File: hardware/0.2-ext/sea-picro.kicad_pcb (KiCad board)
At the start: 4 copper layers, 17.8 x 33 mm, 54 parts, among them J1 USB_C_Receptacle_USB2.0, J2 0.1" x 12, J3 0.1" x 12, J4 D+, J5 D-, J6 0.1" x 5, Q1 2N7002VC-7, Q2 2N7002VC-7, U1 ME6211C33M5G-N, U2 GD25Q64CWIGR, U3 RP2040, Y1 12MHz

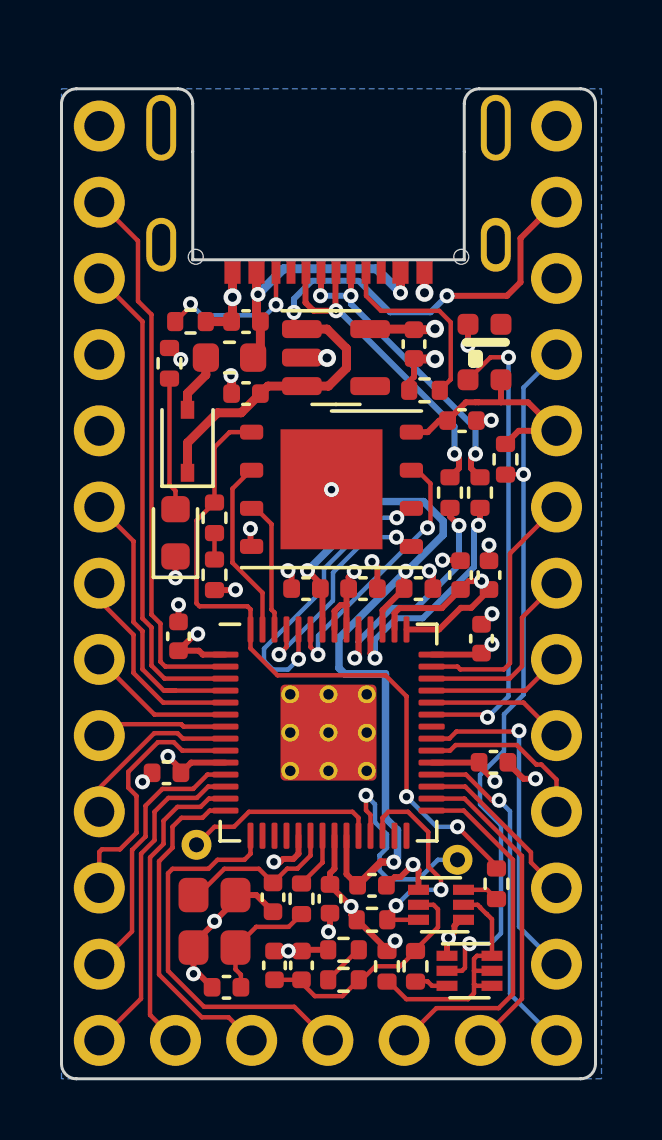
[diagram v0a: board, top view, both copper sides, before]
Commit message: add usb vbus detect
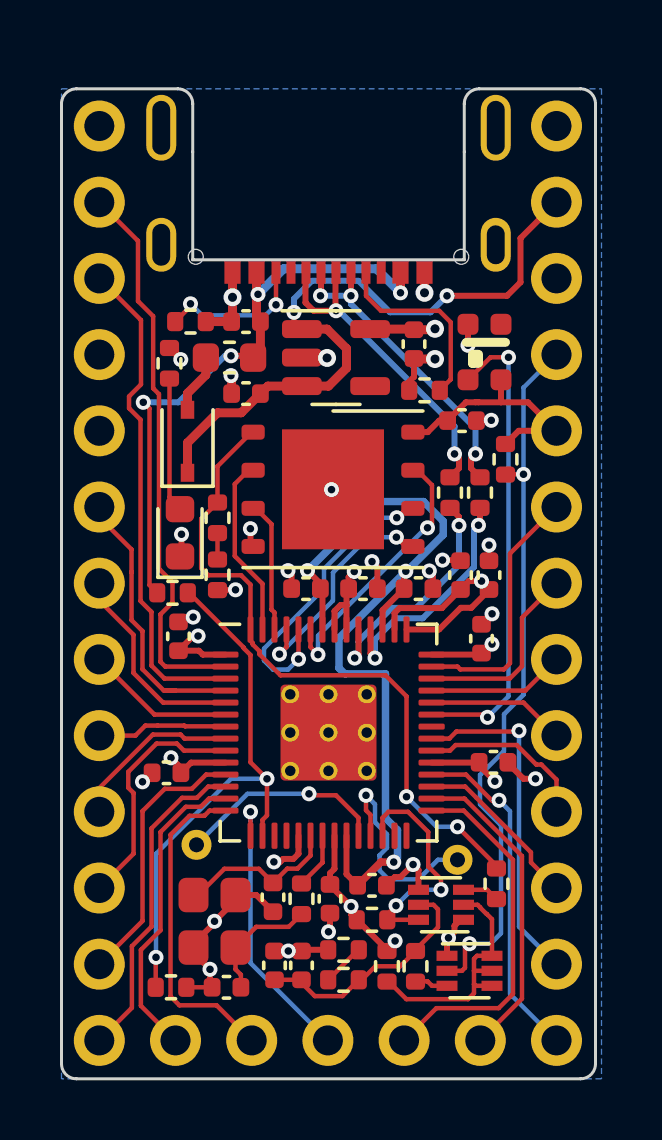
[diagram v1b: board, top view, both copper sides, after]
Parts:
- added R16: 2K2, Resistor_SMD:R_0402_1005Metric, F.Cu at (121.0, 91.6)
- added R17: 5K1, Resistor_SMD:R_0402_1005Metric, F.Cu at (121.0, 104.8)
- R3: value 1K -> 2K2
- moved D2 0.15 mm to (121.2, 89.6)
- moved R10 0.10 mm to (122.5, 89.1)
- moved R6 0.10 mm to (122.5, 91.0)
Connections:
- U3 pad 16: unconnected-(U3-Pad16) -> /VBUS_DETECT
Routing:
- net /VBUS_DETECT: track 0.00 -> 18.5 mm, vias 0 -> 2
- net VBUS: track 9.15 -> 20.0 mm, vias 2 -> 4
- net /15: track 13.2 -> 9.49 mm, vias 0 -> 1
- net /FLASH_nCS: track 23.3 -> 22.4 mm
- net GND: track 28.1 -> 28.8 mm
- net /SWDCLK: track 6.54 -> 7.03 mm, vias 0 -> 1

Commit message: add LED driver and more test points
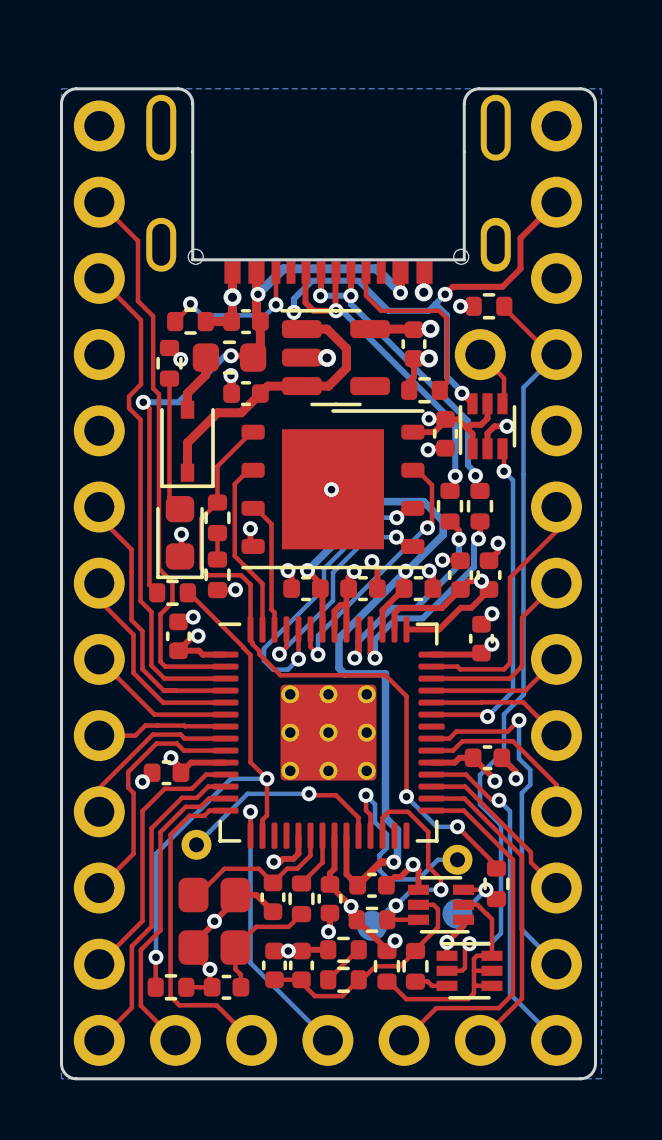
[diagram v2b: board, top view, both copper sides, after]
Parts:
- removed D3: WS2812C-2020, josh-led:WS2812C-2020
- added J7: 2.54, josh-connectors:PinHeader_1x01_P2.54mm_Circle, F.Cu at (131.3, 83.7)
- added TP3: nRST, josh-test-point:TestPoint_SMDPad_D1.0mm_NO_SILK, B.Cu at (127.7, 102.7)
- added TP4: BOOT, josh-test-point:TestPoint_SMDPad_D1.0mm_NO_SILK, B.Cu at (130.5, 102.3)
- added U4: 74LVC1T45Z6-7, Package_TO_SOT_SMD:SOT-563, F.Cu at (131.5, 86.0)
- moved R4 5.13 mm to (131.6, 82.0), turned to 0 degrees
- moved C4 0.70 mm to (130.1, 86.3), turned to -90 degrees
- moved R7 0.45 mm to (130.2, 88.7)
- moved R8 0.45 mm to (131.2, 88.7)
- moved C14 0.25 mm to (131.5, 97.1)
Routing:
- net /LED_DO: track 15.9 -> 11.3 mm
- net +5V: track 22.7 -> 26.2 mm, vias 2 -> 3
- net +3V3: track 36.9 -> 33.8 mm, vias 11 -> 13
- net Net-(J7-Pad1): track 0.00 -> 1.97 mm
- net /SWITCH: track 23.9 -> 25.8 mm, vias 2 -> 1
- net /BOOT: track 1.23 -> 2.51 mm, vias 0 -> 1
- net /nRST: track 7.94 -> 9.02 mm
- net /23_MOSI: track 11.3 -> 12.0 mm
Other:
- board text added: "25"
- board text added: "B"
- board text added: "R"

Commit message: update vscore markings
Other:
- board text added: "<- V score along these lines -> note USB connector sticks out 2mm"
- board text removed: "<- Vscore along -> these edges if panelising"
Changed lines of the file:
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@@
   (gr_line (start 119.75 77.25) (end 119.25 76.75) (layer "B.SilkS") (width 0.15))
   (gr_line (start 133.15 76.7) (end 132.95 76.9) (layer "B.SilkS") (width 0.15))
-  (gr_line (start 135.1 68.5) (end 135.1 114) (layer "Dwgs.User") (width 0.1))
-  (gr_line (start 117.3 68.5) (end 117.3 114) (layer "Dwgs.User") (width 0.1))
+  (gr_line (start 112 107.8) (end 136 107.8) (layer "Dwgs.User") (width 0.1))
+  (gr_line (start 112 74.8) (end 136 74.8) (layer "Dwgs.User") (width 0.1))
   (gr_line (start 117.3 75.3) (end 117.3 107.3) (layer "Edge.Cuts") (width 0.1))
   (gr_line (start 117.8 107.8) (end 134.6 107.8) (layer "Edge.Cuts") (width 0.1))
@@
     (effects (font (size 1 1) (thickness 0.15)) (justify mirror))
   )
-  (gr_text "<- Vscore along ->\nthese edges if\npanelising" (at 126.1 70.7) (layer "Dwgs.User")
+  (gr_text "<- V score along these lines ->\nnote USB connector sticks out 2mm" (at 114.2 91 90) (layer "Dwgs.User")
     (effects (font (size 1 1) (thickness 0.15)))
   )

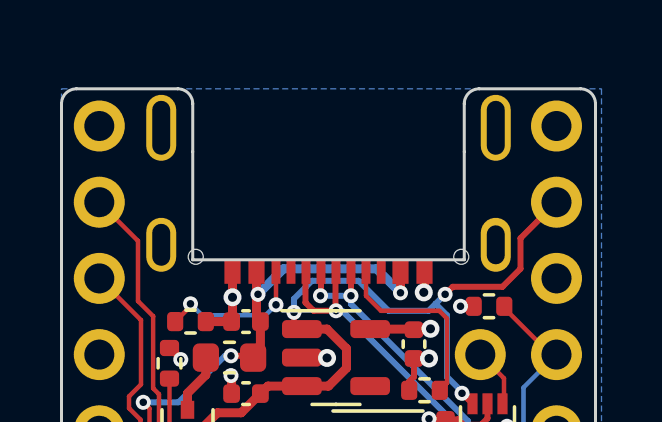
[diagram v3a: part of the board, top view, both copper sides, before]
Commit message: update ldo caps to 1u
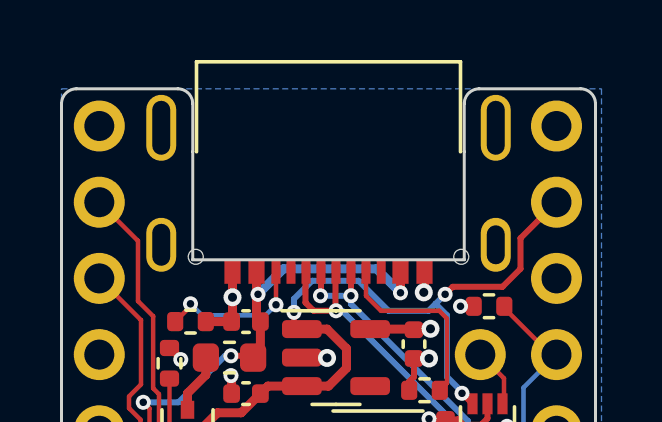
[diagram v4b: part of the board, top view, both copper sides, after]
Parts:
- C12, C9: value 2u2 -> 1u
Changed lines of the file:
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@@
       (effects (font (size 0.75 0.75) (thickness 0.1)))
     )
-    (fp_line (start -4.525 6.6) (end 4.525 6.6) (layer "Edge.Cuts") (width 0.1))
+    (fp_line (start 4.4 0) (end -4.4 0) (layer "F.SilkS") (width 0.12))
+    (fp_line (start -4.4 0) (end -4.4 3) (layer "F.SilkS") (width 0.12))
+    (fp_line (start 4.4 3) (end 4.4 0) (layer "F.SilkS") (width 0.12))
     (fp_line (start -4.525 3) (end -4.525 6.6) (layer "Edge.Cuts") (width 0.1))
     (fp_line (start 4.525 3) (end 4.525 6.6) (layer "Edge.Cuts") (width 0.1))
+    (fp_line (start -4.525 6.6) (end 4.525 6.6) (layer "Edge.Cuts") (width 0.1))
+    (pad "" np_thru_hole circle (at 4.425 6.5) (size 0.5 0.5) (drill 0.5) (layers F&B.Cu *.Mask))
+    (pad "" np_thru_hole circle (at -4.425 6.5) (size 0.5 0.5) (drill 0.5) (layers F&B.Cu *.Mask))
+    (pad "" smd roundrect (at -5.825 2.2) (size 1.5 2.2) (layers "F.Paste") (roundrect_rratio 0.2))
+    (pad "" smd roundrect (at 5.825 6.1) (size 1.5 1.8) (layers "F.Paste") (roundrect_rratio 0.2))
     (pad "" smd roundrect (at -5.825 6.1) (size 1.5 1.8) (layers "F.Paste") (roundrect_rratio 0.2))
-    (pad "" smd roundrect (at 5.825 6.1) (size 1.5 1.8) (layers "F.Paste") (roundrect_rratio 0.2))
     (pad "" smd roundrect (at 5.8 2.2) (size 1.5 2.2) (layers "F.Paste") (roundrect_rratio 0.2))
-    (pad "" np_thru_hole circle (at -4.425 6.5) (size 0.5 0.5) (drill 0.5) (layers F&B.Cu *.Mask))
-    (pad "" np_thru_hole circle (at 4.425 6.5) (size 0.5 0.5) (drill 0.5) (layers F&B.Cu *.Mask))
-    (pad "" smd roundrect (at -5.825 2.2) (size 1.5 2.2) (layers "F.Paste") (roundrect_rratio 0.2))
+    (pad "A1" smd rect (at 3.2 7) (size 0.54 0.8) (layers "F.Cu" "F.Paste" "F.Mask")
+      (net 1 "GND") (pinfunction "GND") (pintype "power_in") (clearance 0.15))
     (pad "A1" smd rect (at -3.2 7) (size 0.54 0.8) (layers "F.Cu" "F.Paste" "F.Mask")
-      (net 1 "GND") (pinfunction "GND") (pintype "power_in") (clearance 0.15))
-    (pad "A1" smd rect (at 3.2 7) (size 0.54 0.8) (layers "F.Cu" "F.Paste" "F.Mask")
       (net 1 "GND") (pinfunction "GND") (pintype "power_in") (clearance 0.15))
     (pad "A4" smd rect (at 2.4 7) (size 0.54 0.8) (layers "F.Cu" "F.Paste" "F.Mask")
@@
     (tags "capacitor")
     (property "JLC Basic" "Y")
-    (property "LCSC" "C12530")
-    (property "MPN " "CL05A225MQ5NSNC")
+    (property "LCSC" "C15849")
+    (property "MPN " "CL10A105KB8NNNC")
     (property "Manufacturer" "Samsung Electro-Mechanics")
     (property "Sheetfile" "sea-picro.kicad_sch")
@@
       (effects (font (size 1 1) (thickness 0.15)))
     )
-    (fp_text value "2u2" (at 0 1.16) (layer "F.Fab") hide
+    (fp_text value "1u" (at 0 1.16) (layer "F.Fab") hide
       (effects (font (size 1 1) (thickness 0.15)))
     )
@@
     (tags "capacitor")
     (property "JLC Basic" "Y")
-    (property "LCSC" "C12530")
-    (property "MPN " "CL05A225MQ5NSNC")
+    (property "LCSC" "C15849")
+    (property "MPN " "CL10A105KB8NNNC")
     (property "Manufacturer" "Samsung Electro-Mechanics")
     (property "Sheetfile" "sea-picro.kicad_sch")
@@
       (effects (font (size 1 1) (thickness 0.15)))
     )
-    (fp_text value "2u2" (at 0 1.16) (layer "F.Fab") hide
-      (effects (font (size 1 1) (thickness 0.15)))
-    )
+    (fp_text value "1u" (at 0 1.16) (layer "F.Fab") hide
+      (effects (font (size 1 1) (thickness 0.15)))
+    )

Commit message: fixes after assembly
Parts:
- U1: value ME6211C33M5G-N -> AP7365-33WG-7
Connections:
- net /15 renamed /12
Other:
- board text added: "PIN 12 LABELED INCORRECTLY ON BACK SILK"
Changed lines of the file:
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@@
   (net 46 "/D-")
   (net 47 "/SWITCH")
-  (net 48 "/15")
+  (net 48 "/12")
   (net 49 "Net-(C19-Pad1)")
   (net 50 "unconnected-(U3-Pad28)")
@@
     (tags "SOT TO_SOT_SMD")
     (property "JLC Basic" "N")
-    (property "LCSC" "C82942")
-    (property "MPN " "ME6211C33M5G-N")
-    (property "Manufacturer" "MICRONE(Nanjing Micro One Elec)")
+    (property "LCSC" "C150742")
+    (property "MPN " "AP7365-33WG-7 ")
+    (property "Manufacturer" "Diodes Incorporated")
     (property "Sheetfile" "sea-picro.kicad_sch")
     (property "Sheetname" "")
@@
       (effects (font (size 1 1) (thickness 0.15)))
     )
-    (fp_text value "ME6211C33M5G-N" (at 0 2.4) (layer "F.Fab") hide
+    (fp_text value "AP7365-33WG-7 " (at 0 2.4) (layer "F.Fab") hide
       (effects (font (size 1 1) (thickness 0.15)))
     )
@@
       (net 58 "/11") (pinfunction "Pin_2") (pintype "passive"))
     (pad "3" thru_hole oval (at 0 5.08 90) (size 1.7 1.7) (drill 1) (layers *.Cu *.Mask)
-      (net 48 "/15") (pinfunction "Pin_3") (pintype "passive"))
+      (net 48 "/12") (pinfunction "Pin_3") (pintype "passive"))
     (pad "4" thru_hole oval (at 0 7.62 90) (size 1.7 1.7) (drill 1) (layers *.Cu *.Mask)
       (net 59 "/18") (pinfunction "Pin_4") (pintype "passive"))
@@
       (net 58 "/11") (pinfunction "GPIO11") (pintype "bidirectional"))
     (pad "15" smd roundrect (at -2.6 3.4375) (size 0.2 0.875) (layers "F.Cu" "F.Paste" "F.Mask") (roundrect_rratio 0.25)
-      (net 48 "/15") (pinfunction "GPIO12") (pintype "bidirectional"))
+      (net 48 "/12") (pinfunction "GPIO12") (pintype "bidirectional"))
     (pad "16" smd roundrect (at -2.2 3.4375) (size 0.2 0.875) (layers "F.Cu" "F.Paste" "F.Mask") (roundrect_rratio 0.25)
       (net 56 "/VBUS_DETECT") (pinfunction "GPIO13") (pintype "bidirectional"))
@@
     (effects (font (size 1 1) (thickness 0.15)))
   )
+  (gr_text "PIN 12 LABELED\nINCORRECTLY ON \nBACK SILK" (at 126.3 110.9) (layer "Dwgs.User")
+    (effects (font (size 1 1) (thickness 0.15)))
+  )

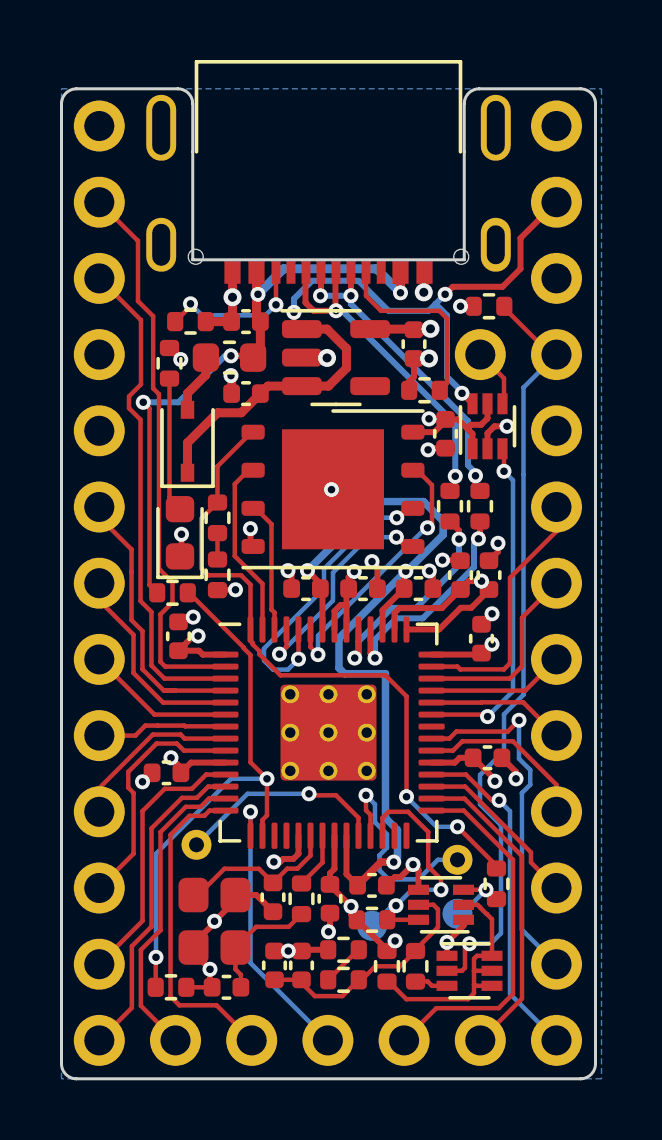
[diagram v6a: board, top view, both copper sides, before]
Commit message: Move Y1, C5, C19
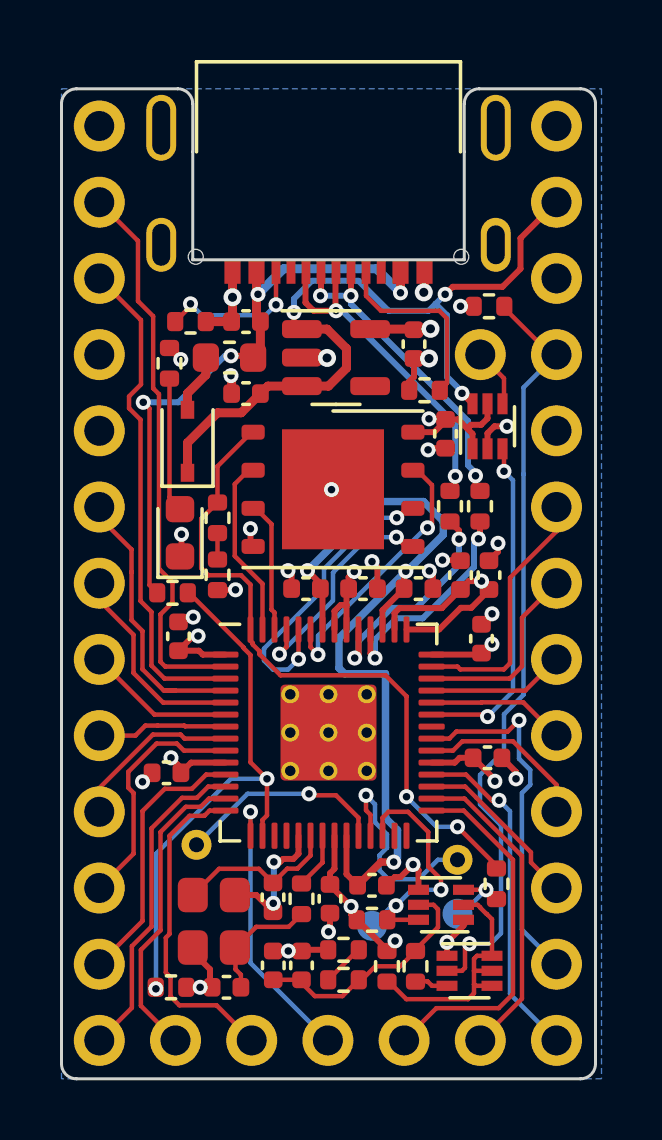
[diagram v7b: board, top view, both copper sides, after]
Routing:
- net GND: track 29.2 -> 28.1 mm
